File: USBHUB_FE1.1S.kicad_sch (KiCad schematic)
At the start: 25 parts, among them J5 Conn_01x04_Socket, U1 FE1.1s, Y1 Crystal_GND24

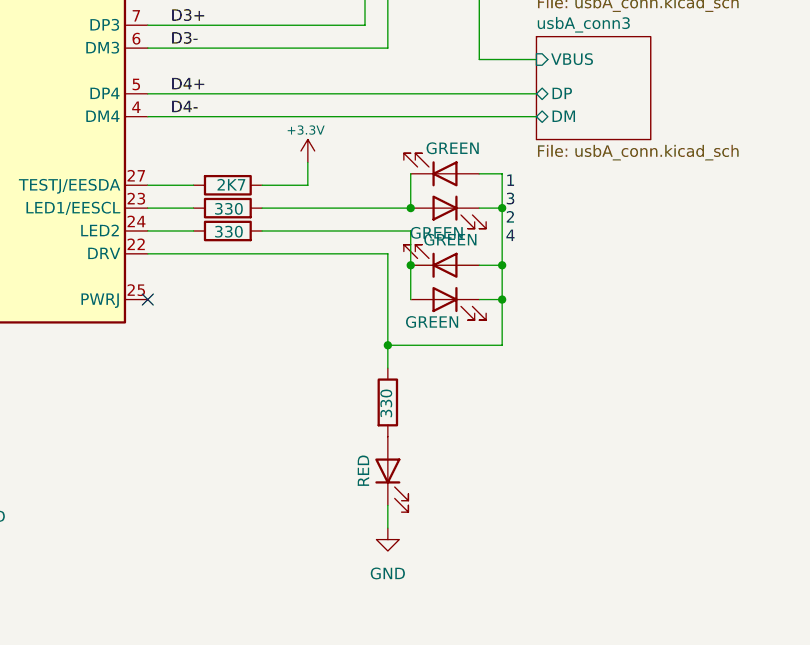
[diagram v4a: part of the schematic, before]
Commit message: Reordering the leds on the board.
They should be in the same order as the ports.
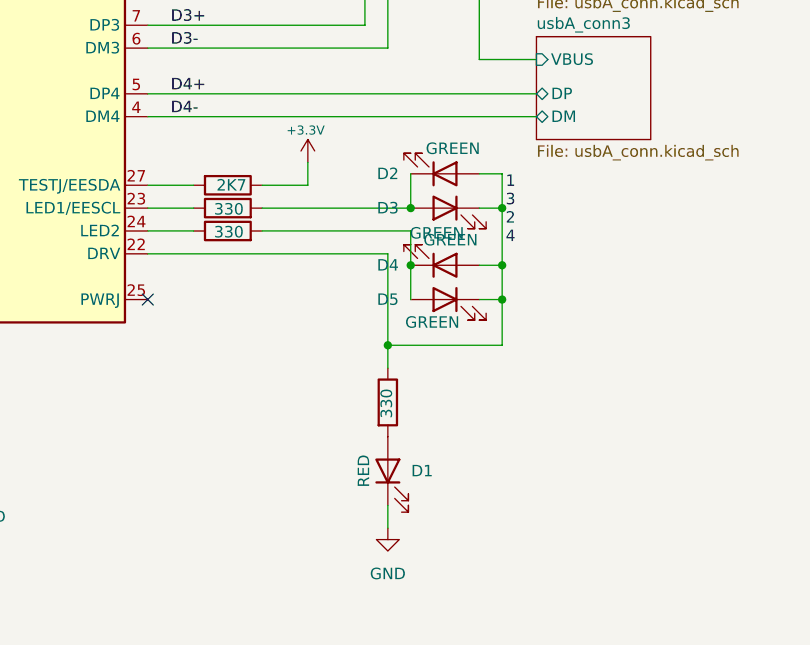
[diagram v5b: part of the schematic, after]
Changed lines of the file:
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@@
   (symbol (lib_id "Device:LED") (at 201.93 105.41 0) (mirror x) (unit 1)
     (in_bom yes) (on_board yes) (dnp no)
-    (property "Reference" "D4" (at 200.3425 97.409 0)
-      (effects (font (size 1.27 1.27)) hide)
+    (property "Reference" "D4" (at 195.58 105.41 0)
+      (effects (font (size 1.27 1.27)))
     )
     (property "Value" "GREEN" (at 202.565 102.616 0)
@@
     )
     (property "Datasheet" "~" (at 201.93 105.41 0)
+      (effects (font (size 1.27 1.27)) hide)
+    )
+    (property "FarnellRef" "" (at 201.93 105.41 0)
       (effects (font (size 1.27 1.27)) hide)
     )
@@
   (symbol (lib_id "Device:LED") (at 201.93 109.22 0) (mirror y) (unit 1)
     (in_bom yes) (on_board yes) (dnp no)
-    (property "Reference" "D5" (at 203.5175 117.221 0)
-      (effects (font (size 1.27 1.27)) hide)
+    (property "Reference" "D5" (at 195.58 109.22 0)
+      (effects (font (size 1.27 1.27)))
     )
     (property "Value" "GREEN" (at 200.533 111.76 0)
@@
     )
     (property "Datasheet" "~" (at 201.93 109.22 0)
+      (effects (font (size 1.27 1.27)) hide)
+    )
+    (property "FarnellRef" "" (at 201.93 109.22 0)
       (effects (font (size 1.27 1.27)) hide)
     )
@@
   (symbol (lib_id "Device:LED") (at 201.93 95.25 0) (mirror x) (unit 1)
     (in_bom yes) (on_board yes) (dnp no)
-    (property "Reference" "D2" (at 200.3425 87.249 0)
-      (effects (font (size 1.27 1.27)) hide)
+    (property "Reference" "D2" (at 195.58 95.25 0)
+      (effects (font (size 1.27 1.27)))
     )
     (property "Value" "GREEN" (at 202.819 92.456 0)
@@
     )
     (property "Datasheet" "~" (at 201.93 95.25 0)
+      (effects (font (size 1.27 1.27)) hide)
+    )
+    (property "FarnellRef" "" (at 201.93 95.25 0)
       (effects (font (size 1.27 1.27)) hide)
     )
@@
   (symbol (lib_id "Device:LED") (at 201.93 99.06 0) (mirror y) (unit 1)
     (in_bom yes) (on_board yes) (dnp no)
-    (property "Reference" "D3" (at 203.5175 107.061 0)
-      (effects (font (size 1.27 1.27)) hide)
+    (property "Reference" "D3" (at 195.58 99.06 0)
+      (effects (font (size 1.27 1.27)))
     )
     (property "Value" "GREEN" (at 201.041 101.854 0)
@@
     )
     (property "Datasheet" "~" (at 201.93 99.06 0)
+      (effects (font (size 1.27 1.27)) hide)
+    )
+    (property "FarnellRef" "" (at 201.93 99.06 0)
       (effects (font (size 1.27 1.27)) hide)
     )
@@
   (symbol (lib_id "Device:LED") (at 195.58 128.27 90) (unit 1)
     (in_bom yes) (on_board yes) (dnp no)
-    (property "Reference" "D1" (at 203.581 129.8575 0)
-      (effects (font (size 1.27 1.27)) hide)
+    (property "Reference" "D1" (at 199.39 128.27 90)
+      (effects (font (size 1.27 1.27)))
     )
     (property "Value" "RED" (at 192.913 128.27 0)
@@
       (effects (font (size 1.27 1.27)) hide)
     )
+    (property "FarnellRef" "" (at 195.58 128.27 0)
+      (effects (font (size 1.27 1.27)) hide)
+    )
